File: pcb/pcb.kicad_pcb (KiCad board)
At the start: 2 copper layers, 77.6 x 97.5 mm, 25 parts, among them J1 Conn_02x04_Odd_Even, J10 Conn_02x04_Odd_Even, J11 Conn_02x04_Odd_Even, J12 Conn_02x04_Odd_Even, J13 Conn_02x04_Odd_Even, J14 Conn_02x04_Odd_Even, J15 Conn_02x04_Odd_Even, J16 Conn_02x04_Odd_Even, J17 Conn_02x04_Odd_Even, J18 Conn_02x04_Odd_Even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

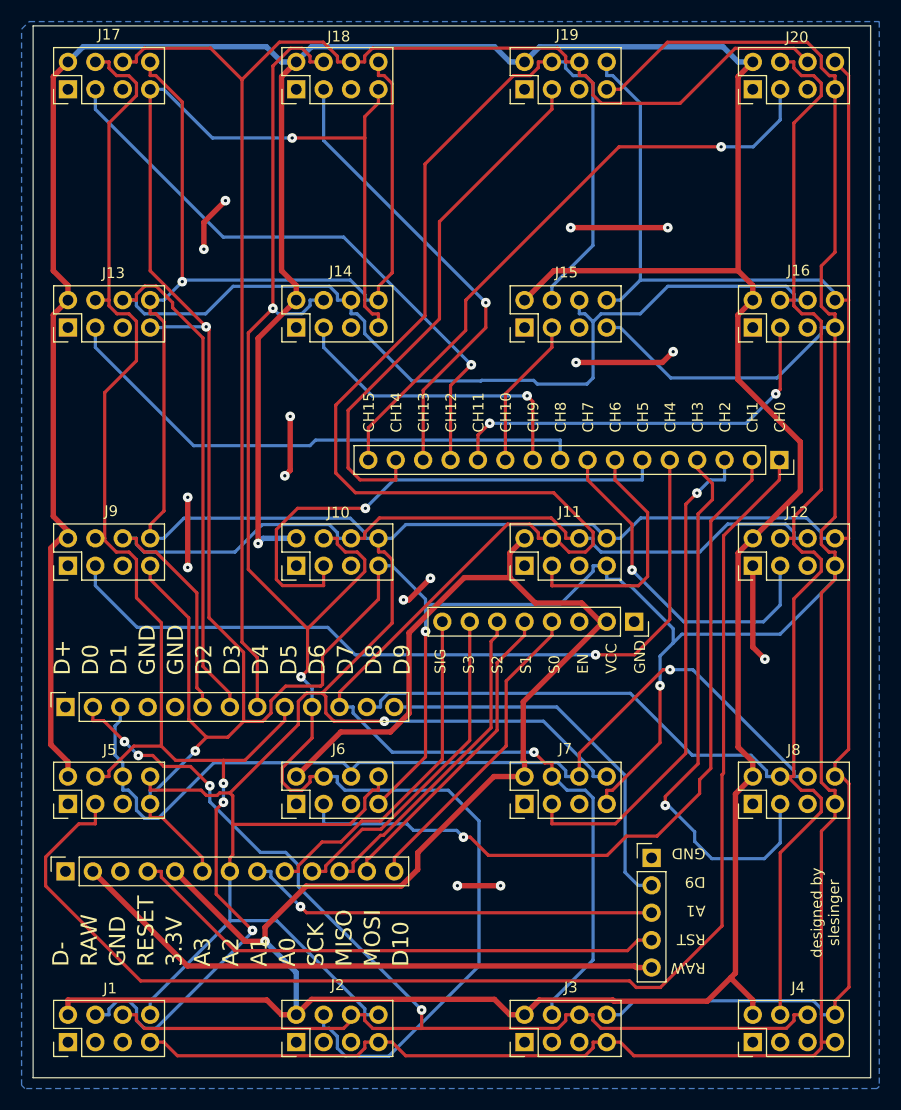
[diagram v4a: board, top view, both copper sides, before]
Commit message: fix multiplexer pin sockets placement
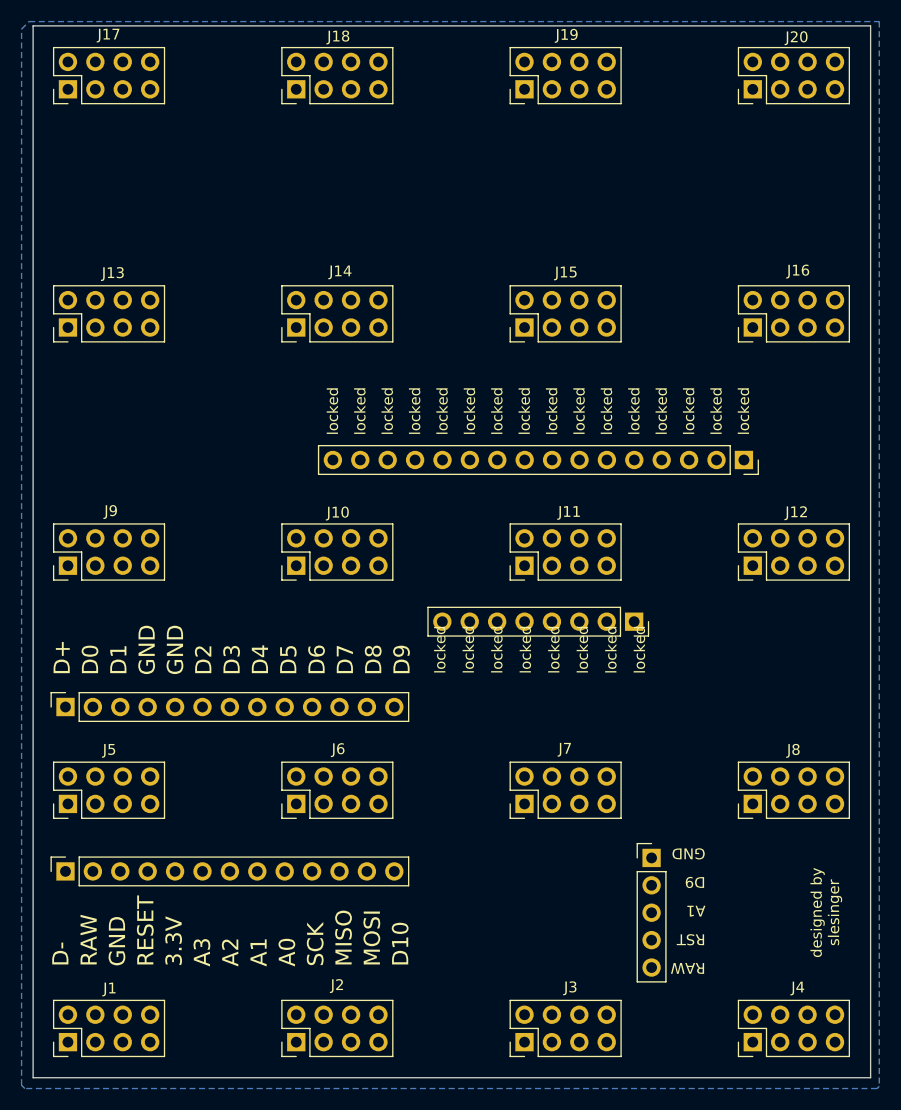
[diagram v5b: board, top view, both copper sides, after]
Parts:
- moved J25 3.29 mm to (65.6, 40.0)
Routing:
- net +3.3V: track 487.7 -> 0.00 mm, vias 2 -> 0
- net Net-(J1-Pin_7): track 479.0 -> 0.00 mm, vias 5 -> 0
- net Net-(J1-Pin_8): track 451.5 -> 0.00 mm, vias 2 -> 0
- net Net-(J11-Pin_4): track 184.7 -> 0.00 mm, vias 1 -> 0
- net Net-(J10-Pin_4): track 152.6 -> 0.00 mm, vias 2 -> 0
- net Net-(J12-Pin_4): track 147.8 -> 0.00 mm
- net Net-(J1-Pin_4): track 136.1 -> 0.00 mm, vias 3 -> 0
- net Net-(J17-Pin_6): track 134.1 -> 0.00 mm
- net Net-(J13-Pin_6): track 127.2 -> 0.00 mm
- net Net-(J25-Pin_1): track 124.8 -> 0.00 mm
- net Net-(J1-Pin_6): track 115.4 -> 0.00 mm, vias 4 -> 0
- net Net-(J10-Pin_6): track 91.2 -> 0.00 mm
- net Net-(J22-Pin_3): track 87.4 -> 0.00 mm, vias 1 -> 0
- net Net-(J25-Pin_5): track 73.9 -> 0.00 mm, vias 1 -> 0
- net Net-(J25-Pin_2): track 73.2 -> 0.00 mm, vias 1 -> 0
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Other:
- board text added: "locked"
- board text removed: "CH0"
- board text removed: "CH1"
- board text removed: "CH10"
- board text removed: "CH11"
- board text removed: "CH12"
- board text removed: "CH13"
- board text removed: "CH14"
- board text removed: "CH15"
- board text removed: "CH2"
- board text removed: "CH3"
- board text removed: "CH4"
- board text removed: "CH5"
- board text removed: "CH6"
- board text removed: "CH7"
- board text removed: "CH8"
- board text removed: "CH9"
- board text removed: "EN"
- board text removed: "S0"
- board text removed: "S1"
- board text removed: "S2"
- board text removed: "S3"
- board text removed: "SIG"
- board text removed: "VCC"

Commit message: updated pcb, 1x1 pcb
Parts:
- moved J4 11.4 mm to (61.3, 83.8)
- moved J3 10.9 mm to (41.3, 83.8)
- moved J2 10.6 mm to (21.3, 83.8)
- moved J1 10.3 mm to (1.27, 83.8)
- moved J21 10.2 mm to (50.3, 69.1), turned to -90 degrees
- moved J8 9.59 mm to (61.3, 63.8)
- moved J22 9.04 mm to (0.94, 54.1)
- moved J23 9.04 mm to (0.94, 69.3)
- moved J7 9.02 mm to (41.3, 63.8)
- moved J6 8.58 mm to (21.3, 63.8)
- moved J5 8.27 mm to (1.27, 63.8)
- moved J12 7.90 mm to (61.3, 43.8)
- moved J11 7.21 mm to (41.3, 43.8)
- moved J10 6.64 mm to (21.3, 43.8)
- moved J16 6.46 mm to (61.3, 23.8)
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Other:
- board size 77.6 x 97.5 mm -> 74.2 x 89.1 mm
- board text removed: "RESET"

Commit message: moved 1x1 pcb folder
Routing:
- net Net-(J1-Pin_7): track 0.00 -> 481.1 mm, vias 0 -> 5
- net Net-(J1-Pin_8): track 0.00 -> 446.2 mm, vias 0 -> 8
- net +3.3V: track 0.00 -> 444.8 mm, vias 0 -> 7
- net Net-(J12-Pin_4): track 0.00 -> 153.5 mm, vias 0 -> 7
- net Net-(J11-Pin_4): track 0.00 -> 147.1 mm, vias 0 -> 4
- net Net-(J1-Pin_4): track 0.00 -> 135.7 mm, vias 0 -> 5
- net Net-(J17-Pin_6): track 0.00 -> 124.2 mm, vias 0 -> 2
- net Net-(J25-Pin_1): track 0.00 -> 118.1 mm, vias 0 -> 6
- net Net-(J10-Pin_4): track 0.00 -> 108.9 mm, vias 0 -> 2
- net Net-(J10-Pin_3): track 0.00 -> 101.2 mm, vias 0 -> 4
- net Net-(J13-Pin_6): track 0.00 -> 100.8 mm, vias 0 -> 1
- net Net-(J10-Pin_6): track 0.00 -> 79.0 mm, vias 0 -> 1
- net Net-(J1-Pin_6): track 0.00 -> 69.3 mm, vias 0 -> 2
- net Net-(J25-Pin_5): track 0.00 -> 65.9 mm, vias 0 -> 2
- net Net-(J20-Pin_3): track 0.00 -> 62.5 mm, vias 0 -> 1
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
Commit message: pcb v2
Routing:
- net Net-(J1-Pin_4): track 135.7 -> 328.5 mm, vias 5 -> 3
- net GND: track 0.00 -> 92.1 mm, vias 0 -> 18
- net Net-(J25-Pin_2): track 20.0 -> 79.5 mm
- net Net-(J1-Pin_6): track 69.3 -> 128.4 mm, vias 2 -> 1
- net Net-(J10-Pin_3): track 101.2 -> 42.7 mm, vias 4 -> 1
- net Net-(J11-Pin_4): track 147.1 -> 179.6 mm, vias 4 -> 5
- net Net-(J23-Pin_13): track 53.7 -> 26.3 mm, vias 4 -> 0
- net Net-(J22-Pin_3): track 59.1 -> 86.5 mm, vias 2 -> 3
- net Net-(J1-Pin_7): track 481.1 -> 453.8 mm
- net Net-(J10-Pin_6): track 79.0 -> 98.7 mm
- net Net-(J23-Pin_11): track 40.6 -> 27.8 mm, vias 3 -> 1
- net Net-(J25-Pin_3): track 62.3 -> 50.3 mm, vias 1 -> 5
- net Net-(J23-Pin_12): track 38.1 -> 27.5 mm, vias 3 -> 0
- net Net-(J12-Pin_4): track 153.5 -> 143.9 mm, vias 7 -> 2
- net Net-(J11-Pin_3): track 9.41 -> 18.7 mm, vias 1 -> 0
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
